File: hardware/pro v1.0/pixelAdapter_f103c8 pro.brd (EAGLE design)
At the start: 26.9 x 34.9 mm, 37 parts, among them U1 SN74HCT245PWR, U2 AP2120N-3.3TRG1, U3 STM32L432KCU6

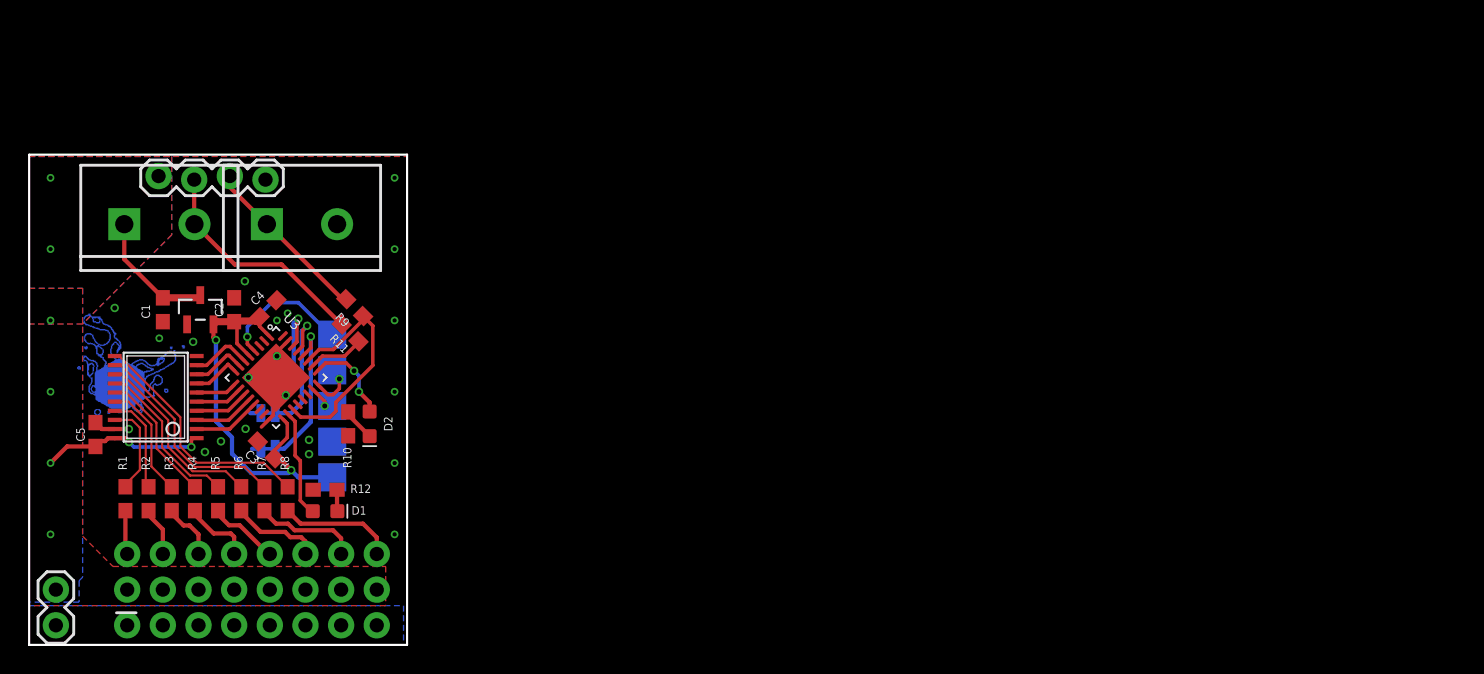
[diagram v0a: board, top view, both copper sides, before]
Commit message: hardware files for variants, limit max transfer bits
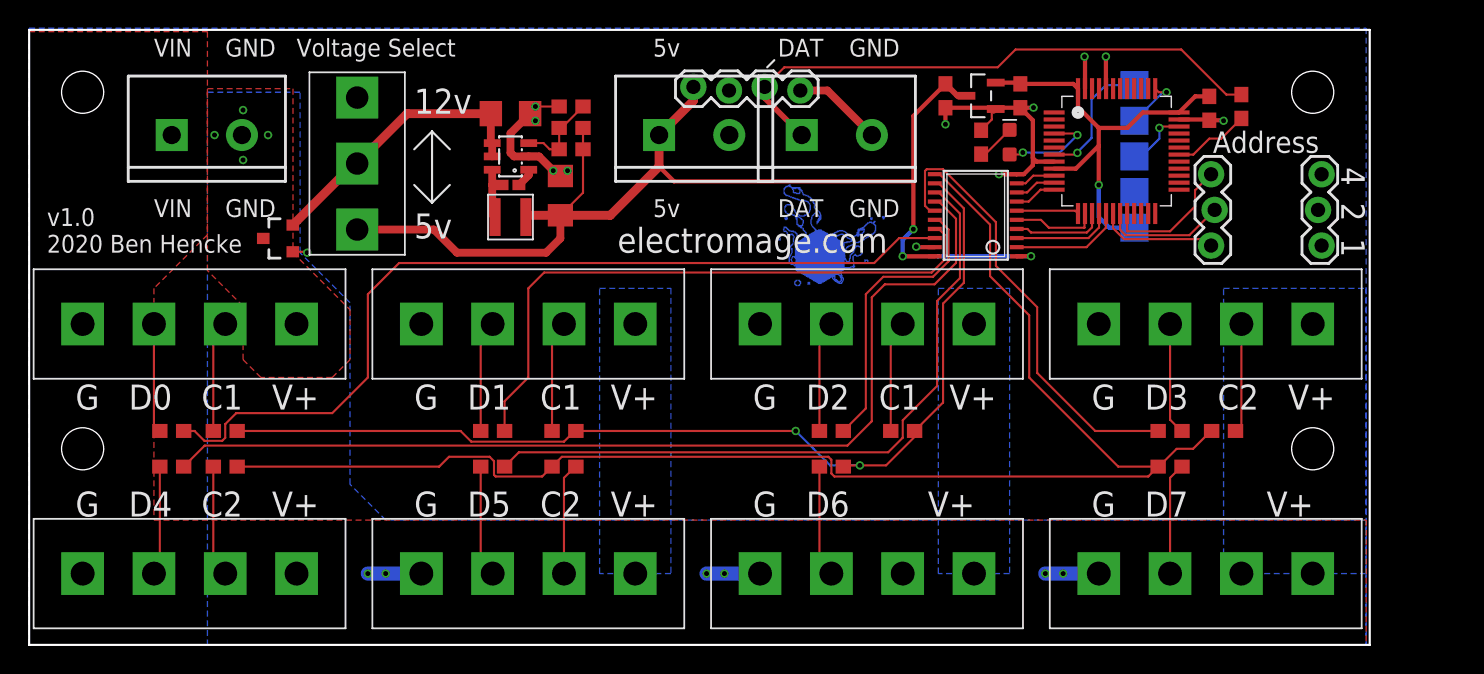
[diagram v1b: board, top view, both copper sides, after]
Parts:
- removed D1: GREEN, SparkFun-LED:LED-0603
- removed JP1, JP2, JP3: JUMPER-SMT_2_NC_TRACE_SILK, SparkFun-Jumpers:SMT-JUMPER_2_NC_TRACE_SILK
- removed U3: STM32L432KCU6, STM32L432KCU6:QFN50P500X500X60-33N
- added C6: 0.1uF, adafruit:C0402K
- added C7: 22pF, SparkFun-Capacitors:0603
- added L2: INDUCTOR3030, bens:INDUCTOR-3030
- added Q3: 2.5A/30V/105mΩ, SparkFun-DiscreteSemi:SOT23-3
- added R13, R14, R15, R16, R17, R18: 75, SparkFun-Resistors:0603
- added U$1: STM32F103C8T6, STM32F103C8T6:LQFP48_7X7MM_0.5MMPP
- added U$10, U$3, U$5, U$6, U$7, U$8, U$9: CON4-508, bens:CON4-508
- added U$11: SWITCH-SPDTXKB-SS-12D10, bens:SWITCH-XKB-SS-12D10
- added U$12: (no value), Electro_Mage_pcb4_pixel_6:ELECTRO_MAGE_PCB4_PIXEL_2#PNG
- added U$4: SY8120B1ABC, bens:SOT23-6
- C1: value 4.7uF -> 1.0uF
- C4: value 0.1uF -> 47uF; device SparkFun-Capacitors:0603 -> SparkFun-Capacitors:1206
- C5: value 0.1uF -> 4.7uF; device SparkFun-Capacitors:0603 -> SparkFun-Capacitors:1206
- D2: value ORANGE -> (none)
- J1: device SparkFun-Connectors:1X08_NO_SILK -> bens:SCREWTERMINAL-5MM-2
- J2: device bens:2X8-NOSILK -> SparkFun-Connectors:1X03_LOCK
- J6: device SparkFun-Connectors:1X02 -> SparkFun-Connectors:1X03_LOCK
- R1, R10, R2, R3, R4, R5, R6, R7, R8, R9: value 100 -> 75
- R11: value 100 -> 100k
- R12: value 100 -> 13.7k
- U$2: value (none) -> CON4-508; device Electro_Mage_pcb4_pixel_6:ELECTRO_MAGE_PCB4_PIXEL_2#PNG -> bens:CON4-508
- moved J6 95.6 mm to (91.9, 33.5), turned to 270 degrees
- moved J2 81.1 mm to (84.3, 28.4), turned to 90 degrees
- moved C3 71.5 mm to (84.1, 38.2), turned to 270 degrees
- moved R4 69.6 mm to (81.3, 15.2), turned to 0 degrees
- moved R9 64.8 mm to (86.4, 38.4), turned to 270 degrees
- moved R8 62.9 mm to (81.3, 12.7), turned to 0 degrees
- moved TP1 59.9 mm to (78.7, 37.3)
- moved TP2 59.9 mm to (78.7, 34.8)
- moved TP3 59.9 mm to (78.7, 32.3)
- moved TP4 59.9 mm to (78.7, 29.7)
- moved TP5 59.9 mm to (78.7, 39.9)
- moved U1 59.8 mm to (67.4, 30.6)
- moved C2 58.0 mm to (70.6, 39.1), turned to 270 degrees
- moved C1 57.8 mm to (65.3, 39.1)
- moved U2 57.7 mm to (67.8, 39.1), turned to 90 degrees
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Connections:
- net DAT_IN renamed N$1
- net N$12 renamed LEDS0
- net N$13 renamed LEDS1
- net N$14 renamed LEDS2
- net N$15 renamed LEDS3
- net N$16 renamed LEDS4
- net N$17 renamed LEDS5
- removed net 5V: C1.1, C5.1, J2.1, J2.11, J2.13, J2.15, J2.3, J2.5, J2.7, J2.9, J3.1, J5.4, J6.2, U1.1, U1.20, U2.3
- removed net CLK: R11.1, U3.26
- removed net CLK_IN: J3.2, J5.3, R11.2
- removed net JP1: JP1.1, U3.30
- removed net JP2: JP2.1, U3.29
- removed net JP3: JP3.2, U3.28
- removed net LED_G: D1.A, U3.18
- removed net LED_O: D2.A, U3.25
- removed net N$18: R7.1, U1.12
- removed net N$19: R8.1, U1.11
- removed net N$2: D1.C, R12.1
- new net +5V: C1.1, C4.1, C7.1, J3.1, J5.4, L2.P$2, R11.2, U$11.P$3, U1.1, U1.20, U2.3
- new net ADDR0: J2.1, U$1.18
- new net ADDR1: J2.2, U$1.19
- new net ADDR2: J2.3, U$1.20
- new net LEDS6: R13.1, R14.1, R15.1, R7.1, U1.12
- new net LEDS7: R16.1, R17.1, R18.1, R8.1, U1.11
- new net N$10: C7.2, R11.1, R12.2, U$4.3
- new net N$11: R15.2, U$5.3
- new net N$20: R16.2, U$6.3
- new net N$22: R17.2, U$7.3
- new net N$23: R18.2, U$8.3
- new net N$3: D2.A, U$1.4
- new net N$6: R13.2, U$2.3
- new net N$7: R14.2, U$3.3
- new net N$8: C6.1, U$4.1
- new net N$9: C6.2, L2.P$1, U$4.6
- new net VIN: J1.2, Q3.3, U$10.4, U$2.4, U$3.4, U$5.4, U$6.4, U$7.4, U$8.4, U$9.4
- new net VIN1: C5.1, Q3.2, U$11.P$2, U$4.4, U$4.5
- net +3V3: now also U$1.36, U$1.48, U$1.9; no longer C4.1, U3.1, U3.17, U3.5
- net CH0: now also U$1.17; no longer U3.13
- net CH1: now also U$1.16; no longer U3.12
- net CH2: now also U$1.15; no longer U3.11
- net CH3: now also U$1.14; no longer U3.10
- net CH4: now also U$1.13; no longer U3.9
- net CH5: now also U$1.12; no longer U3.8
- net CH6: now also U$1.11; no longer U3.7
- net CH7: now also U$1.10; no longer U3.6
- net GND: now also J6.2, J6.3, Q3.1, R12.1, U$1.35, U$1.44, U$1.47, U$1.8, U$10.1, U$2.1, U$3.1, U$4.2, U$5.1, U$6.1, U$7.1, U$8.1, U$9.1; no longer J1.2, J1.3, J1.4, J1.5, J1.6, J1.7, J1.8, JP1.2, JP2.2, JP3.1, R12.2, U3.16, U3.31, U3.32, U3.33
- net LED0: now also U$2.2; no longer J2.2
- net LED1: now also U$3.2; no longer J2.4
- net LED2: now also U$5.2; no longer J2.6
- net LED3: now also U$6.2; no longer J2.8
- net LED4: now also U$7.2; no longer J2.10
- net LED5: now also U$8.2; no longer J2.12
- net LED6: now also U$9.2; no longer J2.14
- net LED7: now also U$10.2; no longer J2.16
- net NRST: now also U$1.7; no longer U3.4
- net RX: now also U$1.30; no longer U3.19, U3.27
- net SWCLK: now also U$1.37; no longer U3.24
- net SWDIO: now also U$1.34; no longer U3.23
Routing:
- net LEDS7: track 0.00 -> 103.2 mm
- net +5V: track 0.00 -> 88.2 mm, vias 0 -> 3
- net LEDS6: track 0.00 -> 73.3 mm, vias 0 -> 2
- net LEDS4: track 11.5 -> 71.4 mm
- net LEDS0: track 6.65 -> 63.8 mm
- net GND: track 10.2 -> 63.6 mm, vias 21 -> 18
- net LEDS1: track 7.08 -> 44.0 mm
- net LEDS5: track 13.5 -> 49.3 mm
- net N$1: track 12.4 -> 40.9 mm
- net LEDS3: track 9.56 -> 32.3 mm
- net 5V: track 21.1 -> 0.00 mm, vias 8 -> 0
- net VIN1: track 0.00 -> 20.5 mm
- net N$19: track 17.4 -> 0.00 mm
- net CLK_IN: track 16.6 -> 0.00 mm
- net N$18: track 15.4 -> 0.00 mm
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- added copper zone on layer 1, net VIN
- added copper zone on layer 16, net VIN
- removed copper zone on layer 1, net 5V
- removed copper zone on layer 16, net 5V
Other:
- board size 26.9 x 34.9 mm -> 95.5 x 43.8 mm
- board text added: "12v"
- board text added: "3v"
- board text added: "5v"
- board text added: "Address"
- board text added: "G D0 C1 V+"
- board text added: "G D1 C1 V+"
- board text added: "G D2 C1 V+"
- board text added: "G D3 C2 V+"
- board text added: "G D4 C2 V+"
- board text added: "G D5 C2 V+"
- board text added: "G D6 V+"
- board text added: "G D7 V+"
- board text added: "VIN"
- board text added: "Voltage Select"
- board text added: "electromage.com"
- board text added: "v1.0 2020 Ben Hencke"
- board text added: "v1.0 2020 Ben Hencke electromage.com"
- board text removed: "0"
- board text removed: "3"
- board text removed: "3V"
- board text removed: "5"
- board text removed: "5V"
- board text removed: "6"
- board text removed: "7"
- board text removed: "Address Setting"
- board text removed: "CLK"
- board text removed: "Data"
- board text removed: "Draw"
- board text removed: "Input"
- board text removed: "JP1"
- board text removed: "JP2"
- board text removed: "JP3"
- board text removed: "Output Expander"
- board text removed: "Programming Pins"
- board text removed: "Status"
- board text removed: "electromage.com Output Expander v3.0 ©2021 Ben Hencke"
- board text removed: "v3.0 ©2021 Ben Hencke"
